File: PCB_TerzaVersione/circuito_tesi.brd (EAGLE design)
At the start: 100 x 80 mm, 57 parts, among them IC1 SCD41-D-R2, Q1 BSS138, Q2 BSS138, Q3 BSS138, Q4 BSS138, U3 MICS-6814, U6 BME280, U7 LIS3DH, Y1 ECS-.327-9-16-TR

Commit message: aggiunte piste
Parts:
- moved R1 2.16 mm to (33.1, 47.3), turned to 90 degrees
- moved R2 2.14 mm to (33.1, 49.6), turned to 270 degrees
- moved U7 1.00 mm to (40.7, 45.1)
- moved R8 0.73 mm to (30.8, 54.2)
- moved U3 0.45 mm to (17.2, 33.3)
- moved R11 0.41 mm to (13.1, 38.4)
- moved OPAMP 0.30 mm to (25.7, 33.6)
- moved R12 0.30 mm to (15.0, 38.3)
- moved R4 0.30 mm to (36.1, 37.4)
- moved BJT 0.20 mm to (18.6, 38.7)
- turned R17 to 270 degrees
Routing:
- net 3.3V: track 3.71 -> 134.3 mm, vias 0 -> 5
- net GND: track 96.7 -> 190.1 mm, vias 0 -> 2
- net SDA: track 0.99 -> 64.3 mm, vias 0 -> 2
- net 5V: track 2.37 -> 64.8 mm, vias 0 -> 2
- net SCL: track 0.00 -> 53.1 mm
- net BJT: track 0.00 -> 36.0 mm
- net 1.8V: track 12.3 -> 43.9 mm, vias 0 -> 1
- net AIN3: track 0.20 -> 28.6 mm
- net LED: track 0.00 -> 22.6 mm, vias 0 -> 2
- net AIN1: track 0.05 -> 18.4 mm
- net N$10: track 0.00 -> 12.1 mm
- net SWDIO: track 0.00 -> 10.5 mm
- net N$6: track 0.00 -> 10.3 mm
- net SCL5: track 0.00 -> 9.47 mm
- net N$13: track 0.20 -> 7.59 mm
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
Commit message: Colleganenti PCB fatti
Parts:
- removed U7: LIS3DH, LIS3DH:PQFN50P300X300X100-16N
- added U1: STMICROELECTRONICS_LIS3DHSTMICROELECTRONICS_LIS3DH_0_0, STMicroelectronics - LIS3DH:STMICROELECTRONICS_LIS3DH_0
- moved C11 1.08 mm to (27.0, 40.6)
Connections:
- new net BATTERY: C9.1, MDBT42Q.8, R19.2, R20.2
- net 3.3V: now also U1.1, U1.14, U1.8; no longer U7.1, U7.14, U7.8
- net AIN4: no longer C9.1, R19.2, R20.2
- net GND: now also U1.10, U1.12, U1.5, U1.7; no longer U7.10, U7.12, U7.5, U7.7
- net P8: no longer MDBT42Q.2
- net SCL: now also U1.4; no longer U7.4
- net SDA: now also U1.6; no longer U7.6
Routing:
- net GND: track 190.1 -> 295.7 mm, vias 2 -> 8
- net BATTERY: track 0.00 -> 13.6 mm, vias 0 -> 1
- net 3.3V: track 134.3 -> 146.9 mm, vias 5 -> 6
- net 1.8V: track 43.9 -> 48.4 mm
- net AIN4: track 3.22 -> 0.00 mm
- net P8: track 3.75 -> 2.98 mm

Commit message: Connessioni OK
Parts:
- moved C11 0.61 mm to (26.4, 40.5)
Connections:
- removed net AIN4: MDBT42Q.5
- net P8: now also MDBT42Q.4
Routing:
- net GND: track 295.7 -> 302.9 mm, vias 8 -> 7
- net N$27: track 28.1 -> 29.4 mm
- net 3.3V: track 146.9 -> 147.4 mm, vias 6 -> 8

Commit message: Cambiato piedino SPS30
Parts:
- removed SPS30: BG306-05-A-1-0400-X-X_REVD, Connet_5_BG306-05-A-1-0400-X-X_REVD:GCT_BG306-05-A-1-0400-X-X_REVD
- added J2: S5B-ZR-SM4A-TF_(LF)_(SN)CONN_S5B-ZR-SM4A-TF_JST, CONN_SMD_5PIN:CONN_S5B-ZR-SM4A-TF_JST
- moved R17 1.08 mm to (20.7, 40.3)
- moved BJT 0.57 mm to (18.2, 39.1)
- moved R2 0.54 mm to (33.3, 50.1)
- moved R1 0.41 mm to (33.2, 47.7)
- moved MDBT42Q 0.30 mm to (20.2, 47.4)
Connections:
- net 5V: now also J2.1; no longer SPS30.1
- net GND: now also J2.4, J2.5; no longer SPS30.4, SPS30.5
- net SCL5: now also J2.3; no longer SPS30.3
- net SDA5: now also J2.2; no longer SPS30.2
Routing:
- net 5V: track 65.1 -> 60.8 mm
- net 3.3V: track 147.4 -> 145.6 mm
- net SCL5: track 9.47 -> 7.92 mm
- net GND: track 302.9 -> 304.4 mm
- net BJT: track 36.0 -> 36.8 mm
- net P8: track 2.59 -> 1.97 mm
- net N$15: track 2.23 -> 1.65 mm
- net SDA: track 64.6 -> 64.1 mm

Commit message: Sistemate alcune piste
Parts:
- moved U3 1.63 mm to (18.8, 33.6)
- moved R11 1.41 mm to (14.5, 38.2)
- moved R17 1.20 mm to (21.9, 40.3)
- moved R12 1.10 mm to (16.1, 38.3)
- moved R4 1.00 mm to (36.0, 38.4)
- moved R6 0.81 mm to (46.2, 38.2)
- moved BJT 0.70 mm to (18.9, 39.1)
- moved OPAMP 0.60 mm to (26.3, 33.6)
- moved Q2 0.58 mm to (46.4, 34.9)
- moved SGP30 0.57 mm to (41.4, 35.3)
- moved C10 0.54 mm to (42.1, 33.1)
- moved Q1 0.45 mm to (36.1, 34.6)
- moved R3 0.41 mm to (39.0, 34.6)
- moved R13 0.30 mm to (29.6, 36.5)
- moved R14 0.30 mm to (29.6, 32.3)
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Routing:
- net BJT: track 36.8 -> 31.2 mm
- net GND: track 304.4 -> 299.8 mm
- net 1.8V: track 48.5 -> 45.8 mm
- net N$27: track 29.4 -> 31.1 mm
- net N$10: track 12.1 -> 10.5 mm
- net N$13: track 7.59 -> 5.98 mm
- net 3.3V: track 145.6 -> 146.6 mm
- net N$6: track 10.3 -> 9.50 mm
- net 5V: track 60.8 -> 60.1 mm
- net N$7: track 5.72 -> 5.16 mm

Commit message: Sistemate piste PCB
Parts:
- moved R2 0.70 mm to (33.3, 50.8)
- moved R9 0.51 mm to (21.6, 58.5)
- moved R1 0.41 mm to (33.3, 48.1)
- moved C11 0.30 mm to (26.7, 40.5)
- moved Q3 0.10 mm to (24.2, 57.3)
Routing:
- net GND: track 299.8 -> 342.7 mm, vias 7 -> 5
- net 3.3V: track 146.6 -> 148.4 mm
- net AIN3: track 28.4 -> 29.3 mm
- net BATTERY: track 13.9 -> 13.0 mm
- net 1.8V: track 45.8 -> 46.6 mm
- added copper zone on layer 1, net GND
- added copper zone on layer 16, net GND

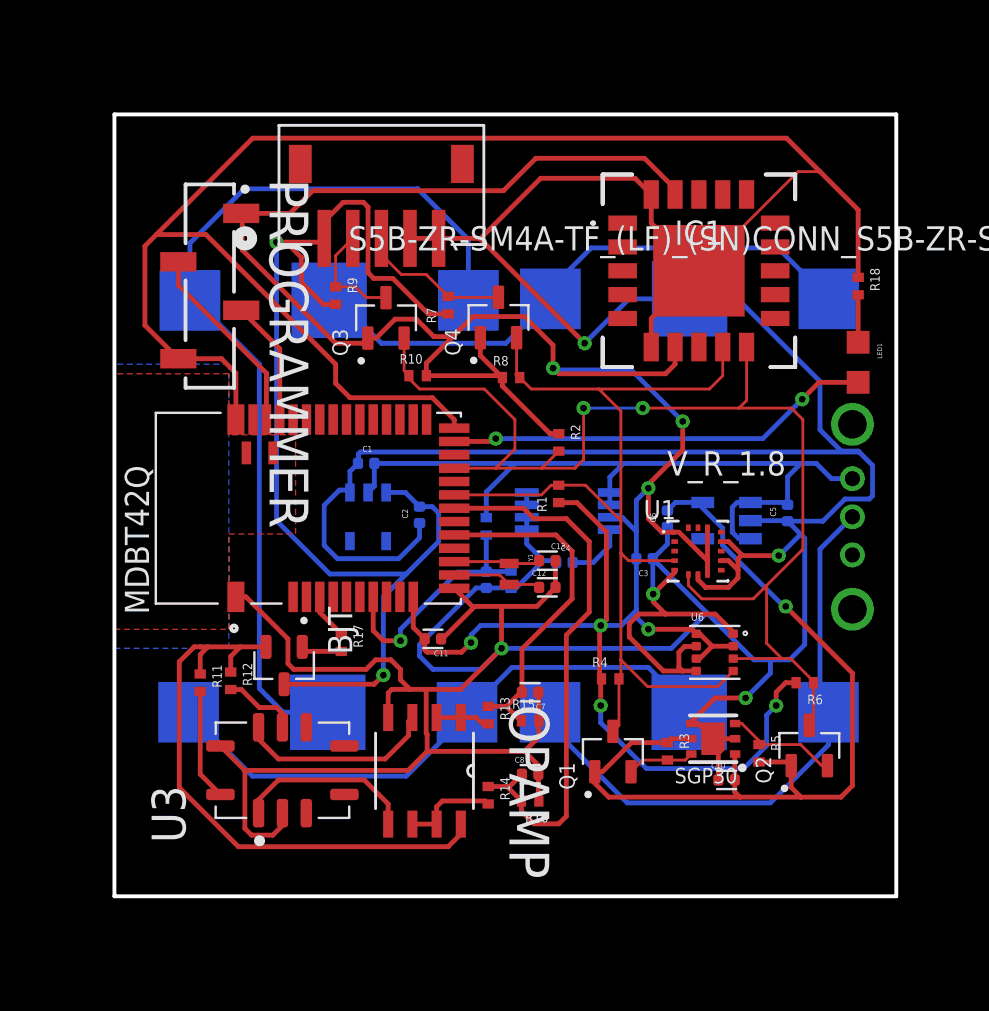
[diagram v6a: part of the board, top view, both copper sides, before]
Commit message: Aggiunti piani di Ground
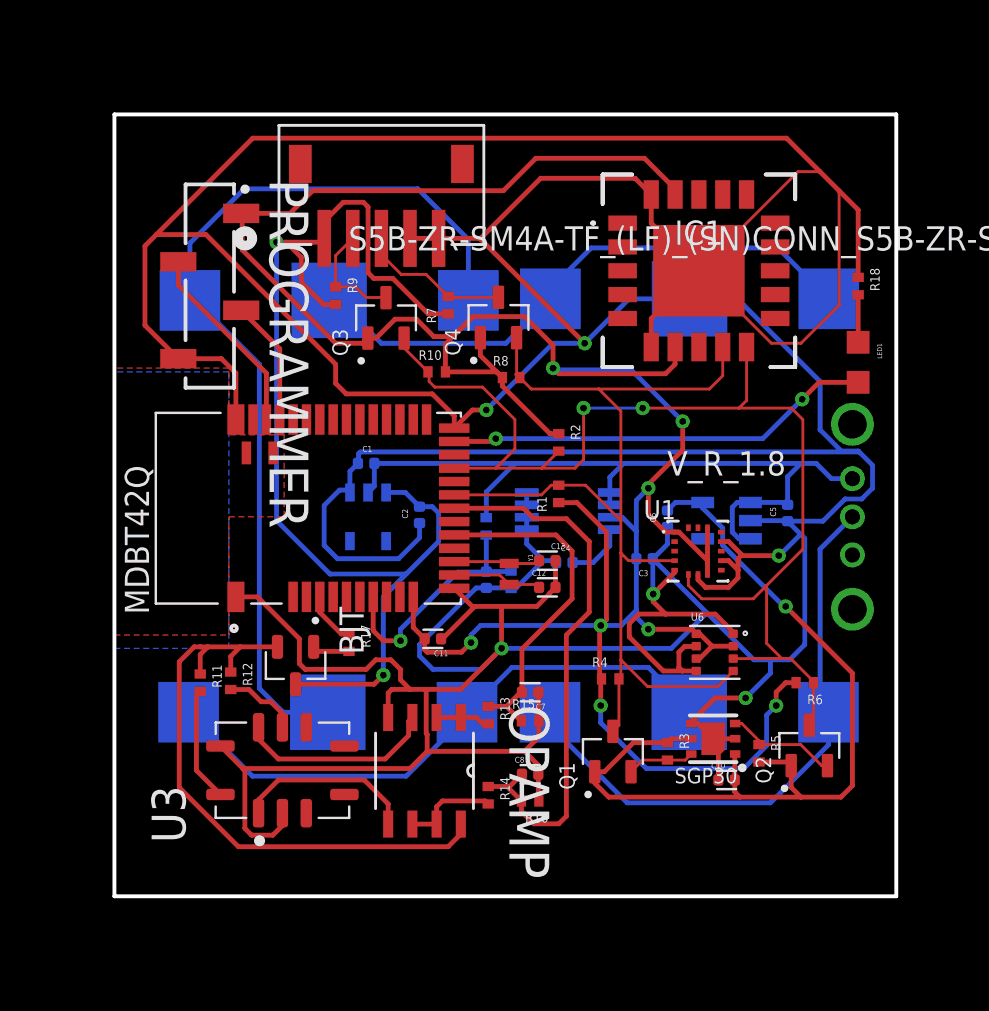
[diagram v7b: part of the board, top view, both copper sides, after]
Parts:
- moved R10 1.02 mm to (26.9, 54.5)
- moved BJT 0.60 mm to (19.5, 39.1)
- moved R17 0.40 mm to (22.3, 40.3)
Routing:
- net GND: track 342.7 -> 367.0 mm, vias 5 -> 6
- net 3.3V: track 148.4 -> 147.0 mm
- net 5V: track 60.4 -> 59.8 mm
- net BJT: track 31.4 -> 32.0 mm
- net SDA: track 63.7 -> 63.2 mm

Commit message: Prototipo finale
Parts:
- moved C5 6.30 mm to (39.0, 47.1)
- moved C6 4.61 mm to (43.0, 44.5), turned to 0 degrees
- moved LED1 0.82 mm to (48.8, 55.8)
- moved R18 0.71 mm to (48.9, 59.7)
- moved V_R_1.8 0.61 mm to (42.0, 47.3), turned to 180 degrees
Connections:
- net 3.3V: now also C5.1, V_R_1.8.1, V_R_1.8.3
- net VDD: no longer C5.1, V_R_1.8.1, V_R_1.8.3
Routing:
- net GND: track 367.0 -> 344.6 mm
- net VDD: track 40.9 -> 33.0 mm
- net 3.3V: track 147.0 -> 154.3 mm
- net 1.8V: track 46.6 -> 42.6 mm
